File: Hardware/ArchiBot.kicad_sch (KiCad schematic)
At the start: 0 parts

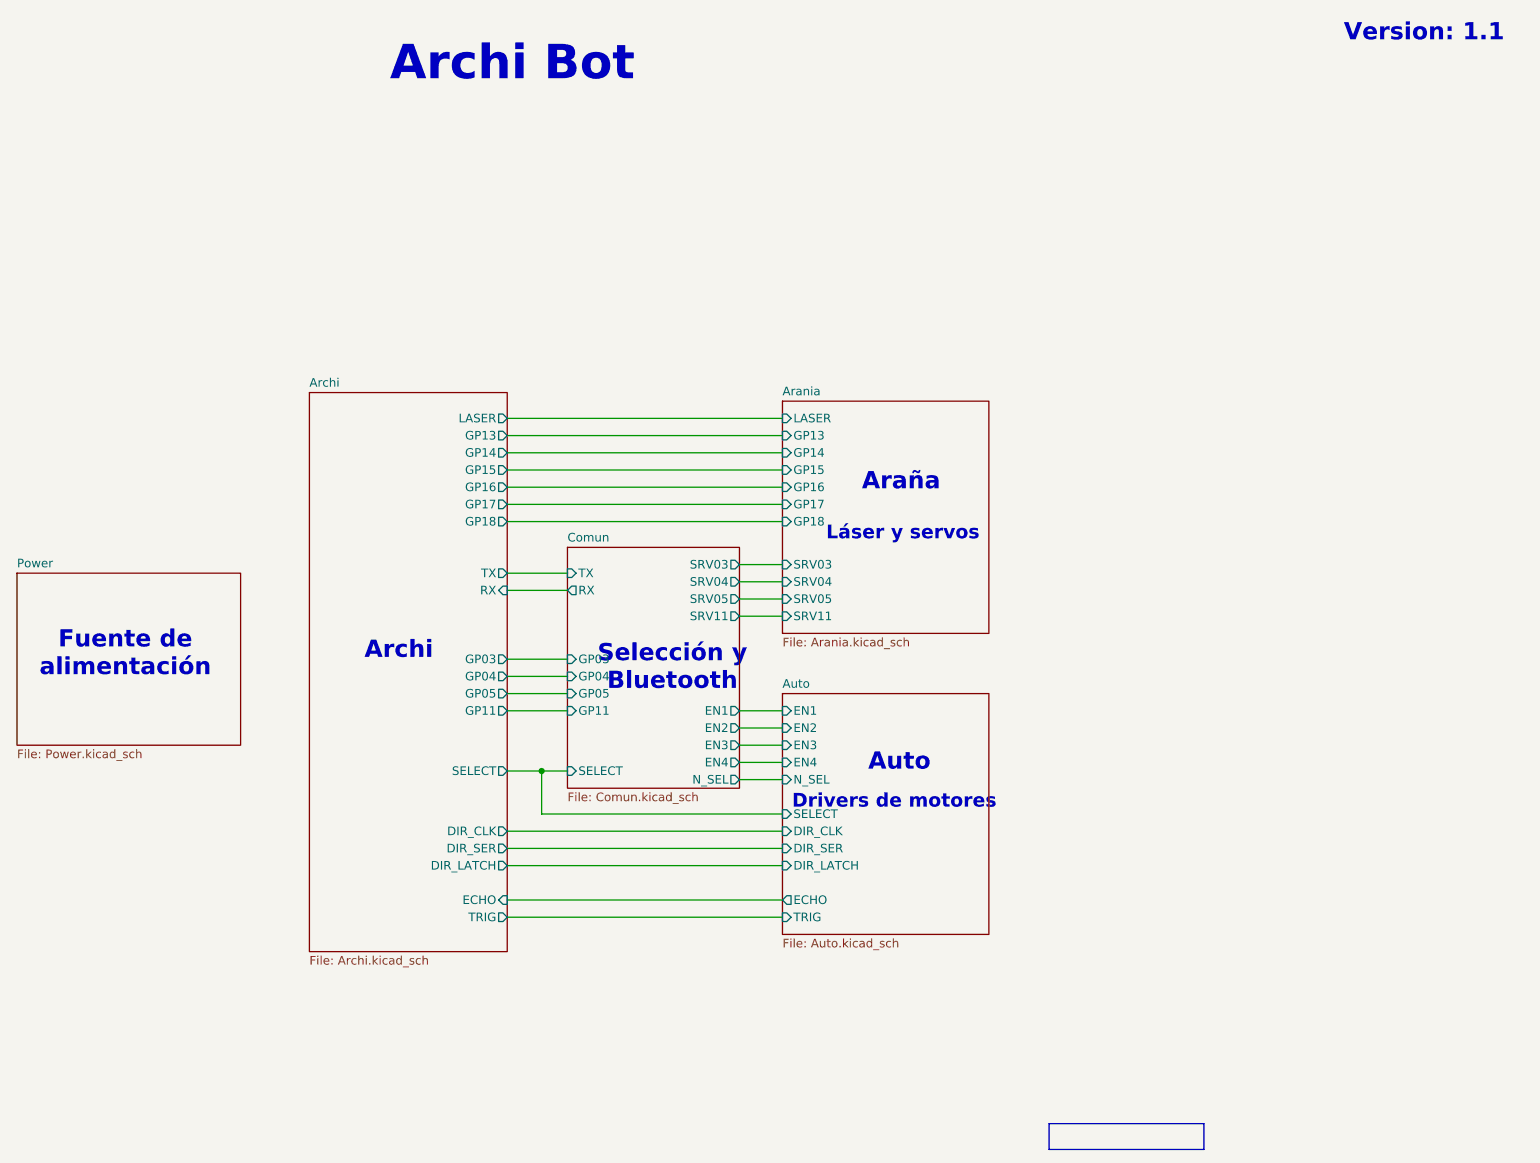
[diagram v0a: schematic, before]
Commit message: Correcciones en el ruteo, agrego fiduciales, 3D y serigrafía
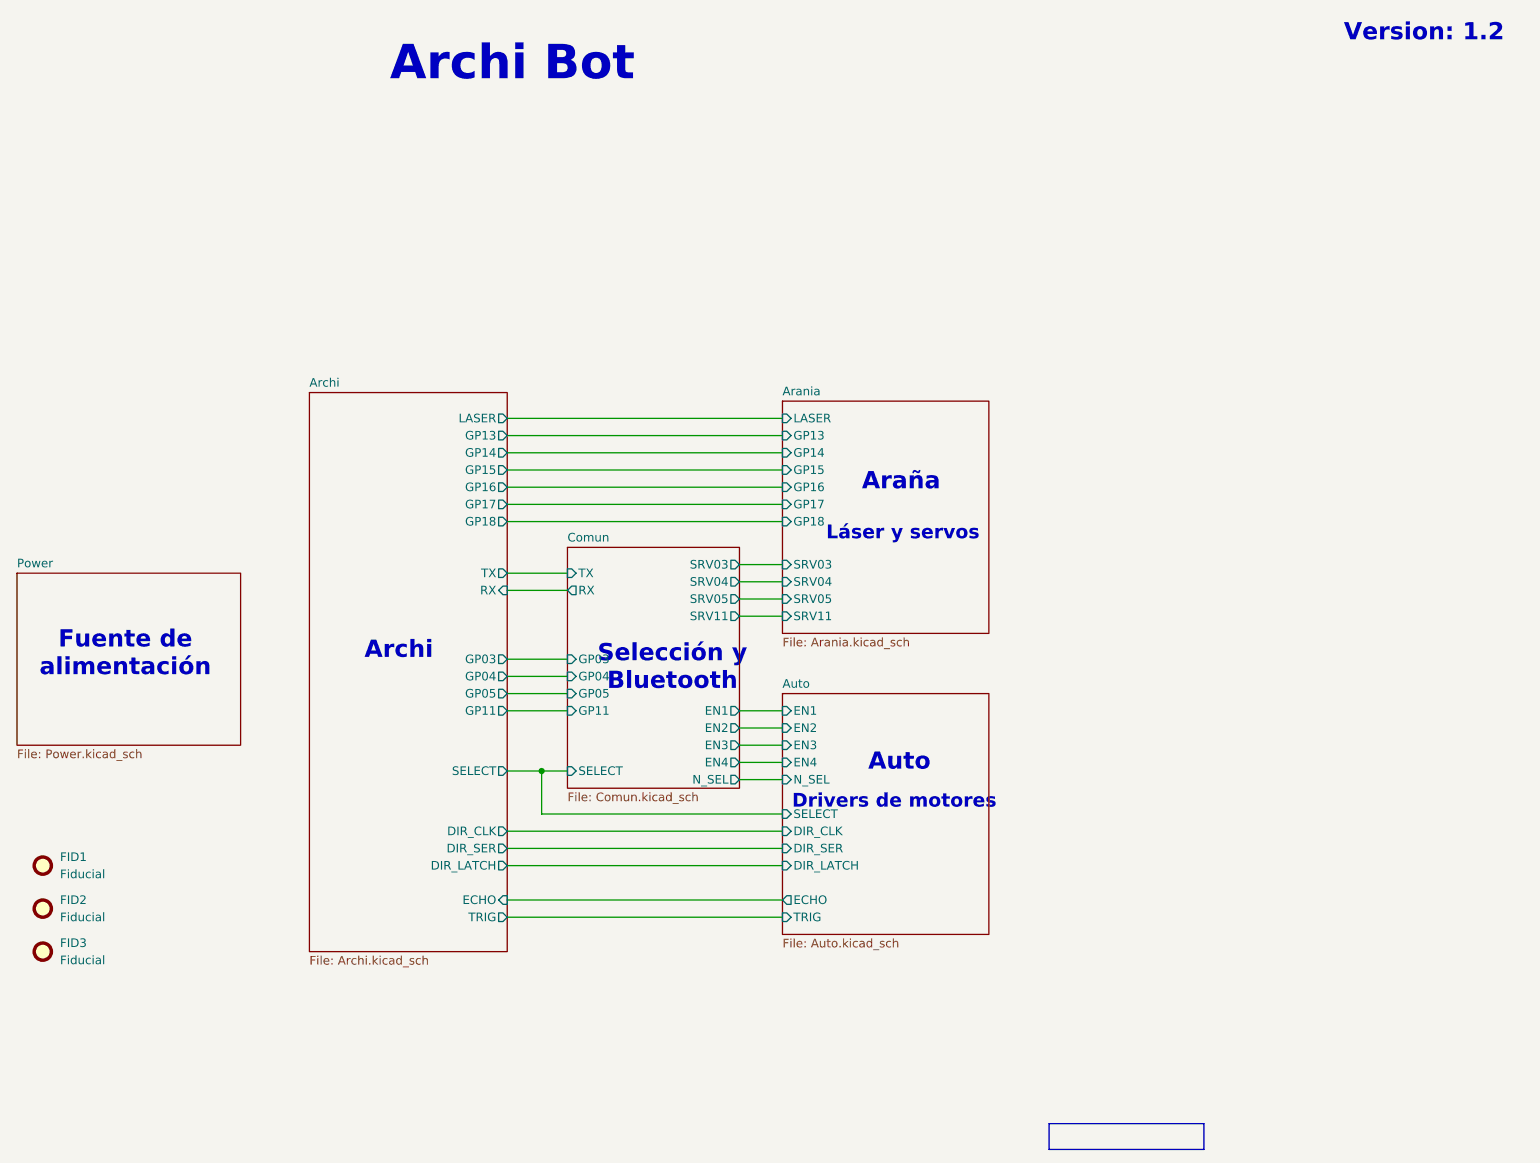
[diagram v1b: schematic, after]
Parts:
- added FID1, FID2, FID3: Fiducial, Fiducial:Fiducial_1mm_Mask2mm, symbol Mechanical:Fiducial
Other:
- company: (none) -> Newsan
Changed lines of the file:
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@@
 	(title_block
 		(title "Archi Bot")
-		(date "2024-07-18")
-		(rev "1.1")
+		(date "2024-09-27")
+		(rev "1.2")
+		(company "Newsan")
 	)
 	(junction
@@
 			)
 		)
+	)
+	(symbol
+		(lib_id "Mechanical:Fiducial")
+		(at 69.85 146.05 0)
+		(unit 1)
+		(exclude_from_sim yes)
+		(in_bom no)
+		(on_board yes)
+		(dnp no)
+		(fields_autoplaced yes)
+		(property "Reference" "FID2"
+			(at 72.39 144.7799 0)
+			(effects
+				(font
+					(size 1.27 1.27)
+				)
+				(justify left)
+			)
+		)
+		(property "Value" "Fiducial"
+			(at 72.39 147.3199 0)
+			(effects
+				(font
+					(size 1.27 1.27)
+				)
+				(justify left)
+			)
+		)
+		(property "Footprint" "Fiducial:Fiducial_1mm_Mask2mm"
+			(at 69.85 146.05 0)
+			(effects
+				(font
+					(size 1.27 1.27)
+				)
+				(hide yes)
+			)
+		)
+		(property "Datasheet" "~"
+			(at 69.85 146.05 0)
+			(effects
+				(font
+					(size 1.27 1.27)
+				)
+				(hide yes)
+			)
+		)
+		(property "Description" "Fiducial Marker"
+			(at 69.85 146.05 0)
+			(effects
+				(font
+					(size 1.27 1.27)
+				)
+				(hide yes)
+			)
+		)
+		(instances
+			(project ""
+				(path "/e63e39d7-6ac0-4ffd-8aa3-1841a4541b55"
+					(reference "FID2")
+					(unit 1)
+				)
+			)
+		)
+	)
+	(symbol
+		(lib_id "Mechanical:Fiducial")
+		(at 69.85 139.7 0)
+		(unit 1)
+		(exclude_from_sim yes)
+		(in_bom no)
+		(on_board yes)
+		(dnp no)
+		(fields_autoplaced yes)
+		(property "Reference" "FID1"
+			(at 72.39 138.4299 0)
+			(effects
+				(font
+					(size 1.27 1.27)
+				)
+				(justify left)
+			)
+		)
+		(property "Value" "Fiducial"
+			(at 72.39 140.9699 0)
+			(effects
+				(font
+					(size 1.27 1.27)
+				)
+				(justify left)
+			)
+		)
+		(property "Footprint" "Fiducial:Fiducial_1mm_Mask2mm"
+			(at 69.85 139.7 0)
+			(effects
+				(font
+					(size 1.27 1.27)
+				)
+				(hide yes)
+			)
+		)
+		(property "Datasheet" "~"
+			(at 69.85 139.7 0)
+			(effects
+				(font
+					(size 1.27 1.27)
+				)
+				(hide yes)
+			)
+		)
+		(property "Description" "Fiducial Marker"
+			(at 69.85 139.7 0)
+			(effects
+				(font
+					(size 1.27 1.27)
+				)
+				(hide yes)
+			)
+		)
+		(instances
+			(project ""
+				(path "/e63e39d7-6ac0-4ffd-8aa3-1841a4541b55"
+					(reference "FID1")
+					(unit 1)
+				)
+			)
+		)
+	)
+	(symbol
+		(lib_id "Mechanical:Fiducial")
+		(at 69.85 152.4 0)
+		(unit 1)
+		(exclude_from_sim yes)
+		(in_bom no)
+		(on_board yes)
+		(dnp no)
+		(fields_autoplaced yes)
+		(property "Reference" "FID3"
+			(at 72.39 151.1299 0)
+			(effects
+				(font
+					(size 1.27 1.27)
+				)
+				(justify left)
+			)
+		)
+		(property "Value" "Fiducial"
+			(at 72.39 153.6699 0)
+			(effects
+				(font
+					(size 1.27 1.27)
+				)
+				(justify left)
+			)
+		)
+		(property "Footprint" "Fiducial:Fiducial_1mm_Mask2mm"
+			(at 69.85 152.4 0)
+			(effects
+				(font
+					(size 1.27 1.27)
+				)
+				(hide yes)
+			)
+		)
+		(property "Datasheet" "~"
+			(at 69.85 152.4 0)
+			(effects
+				(font
+					(size 1.27 1.27)
+				)
+				(hide yes)
+			)
+		)
+		(property "Description" "Fiducial Marker"
+			(at 69.85 152.4 0)
+			(effects
+				(font
+					(size 1.27 1.27)
+				)
+				(hide yes)
+			)
+		)
+		(instances
+			(project ""
+				(path "/e63e39d7-6ac0-4ffd-8aa3-1841a4541b55"
+					(reference "FID3")
+					(unit 1)
+				)
+			)
+		)

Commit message: Actualizo a versión 1.4
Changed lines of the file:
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@@
 	(title_block
 		(title "Archi Bot")
-		(date "2025-05-28")
-		(rev "1.3")
+		(date "2025-06-11")
+		(rev "1.4")
 		(company "Newsan")
 	)
